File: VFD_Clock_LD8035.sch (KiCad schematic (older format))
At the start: 24 parts, among them J1 Conn_01x04, J2 Conn_01x04, J3 CONN_01X05, SW1 SW_Push, SW2 SW_Push, U1 74HC595_Misc, U2 TD62783, U3 TD62783

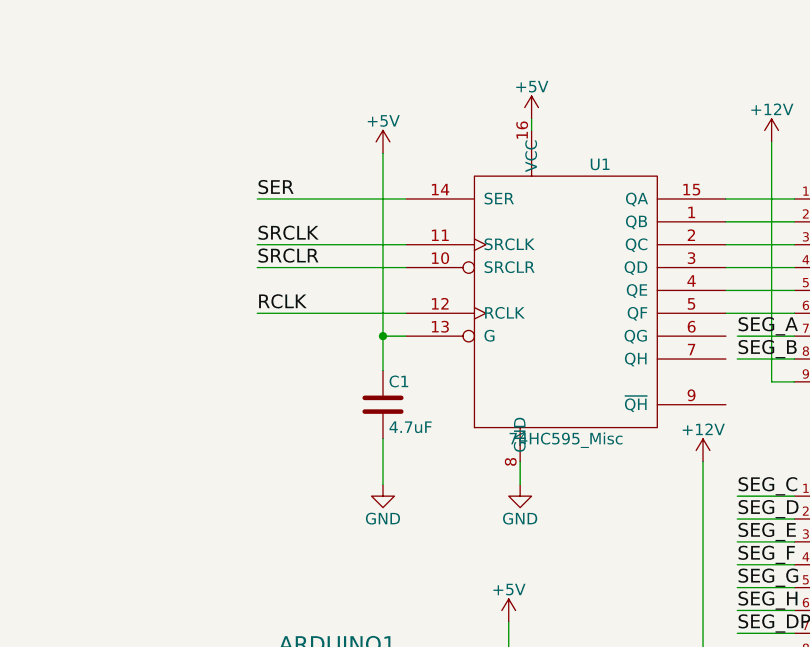
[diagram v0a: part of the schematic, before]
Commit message: Correct connection / Add dummy code
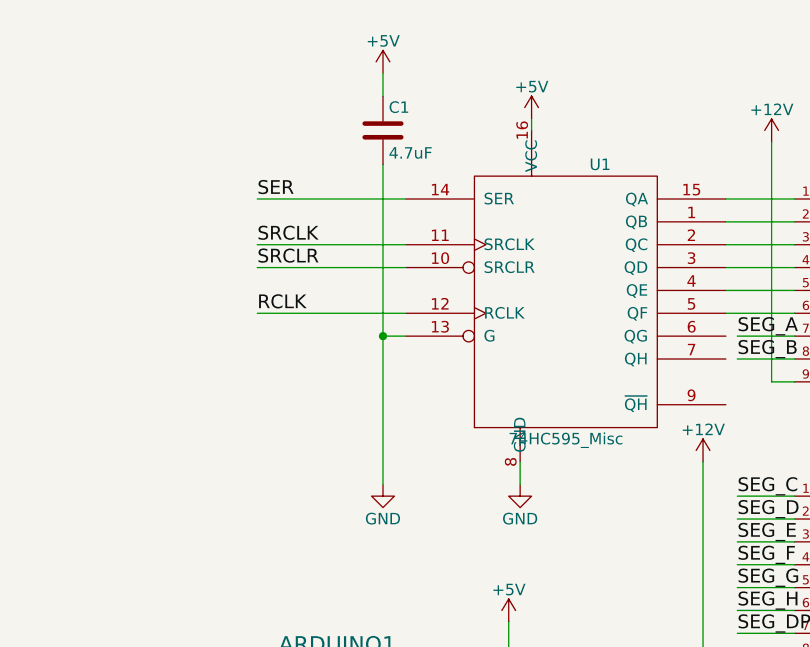
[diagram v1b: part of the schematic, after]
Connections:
- net +5V: no longer U1.13 (G)
- net GND: now also U1.13 (G)
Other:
- moved on the sheet: C1
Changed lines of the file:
@@
 L +5V #PWR019
 U 1 1 5AC41F8D
-P 3800 1050
-F 0 "#PWR019" H 3800 900 50  0001 C CNN
-F 1 "+5V" H 3800 1190 50  0000 C CNN
-F 2 "" H 3800 1050 50  0001 C CNN
-F 3 "" H 3800 1050 50  0001 C CNN
-	1    3800 1050
-	1    0    0    -1
-$EndComp
-Wire Wire Line
-	3800 1050 3800 2000
+P 3800 700
+F 0 "#PWR019" H 3800 550 50  0001 C CNN
+F 1 "+5V" H 3800 840 50  0000 C CNN
+F 2 "" H 3800 700 50  0001 C CNN
+F 3 "" H 3800 700 50  0001 C CNN
+	1    3800 700
+	1    0    0    -1
+$EndComp
 $Comp
 L +5V #PWR020
@@
 L C C1
 U 1 1 5AC4C0A0
-P 3800 2150
-F 0 "C1" H 3825 2250 50  0000 L CNN
-F 1 "4.7uF" H 3825 2050 50  0000 L CNN
-F 2 "Capacitors_THT:C_Disc_D7.5mm_W5.0mm_P5.00mm" H 3838 2000 50  0001 C CNN
-F 3 "" H 3800 2150 50  0001 C CNN
-	1    3800 2150
+P 3800 950
+F 0 "C1" H 3825 1050 50  0000 L CNN
+F 1 "4.7uF" H 3825 850 50  0000 L CNN
+F 2 "Capacitors_THT:C_Disc_D7.5mm_W5.0mm_P5.00mm" H 3838 800 50  0001 C CNN
+F 3 "" H 3800 950 50  0001 C CNN
+	1    3800 950
 	1    0    0    -1
 $EndComp
@@
 $EndComp
 Wire Wire Line
-	3800 2300 3800 2500
+	3800 1100 3800 2500
 $Comp
 L GND #PWR030
@@
 Text Notes 950  6400 0    60   ~ 0
 MT3608 Up Converter 5V to 12V
-Wire Wire Line
-	3900 1850 3800 1850
-Connection ~ 3800 1850
 $Comp
 L 74HC595_Misc U1
@@
 	1    0    0    -1
 $EndComp
+Wire Wire Line
+	3800 800  3800 700
+Wire Wire Line
+	3900 1850 3800 1850
+Connection ~ 3800 1850
 $EndSCHEMATC

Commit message: Changed Resistor to 1/2W
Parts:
- R1, R2, R3, R4, R5, R6: footprint Resistors_THT:R_Axial_DIN0207_L6.3mm_D2.5mm_P2.54mm_Vertical -> Resistors_THT:R_Axial_DIN0309_L9.0mm_D3.2mm_P5.08mm_Vertical
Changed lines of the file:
@@
 F 0 "R1" V 8930 800 50  0000 C CNN
 F 1 "R" V 8850 800 50  0000 C CNN
-F 2 "Resistors_THT:R_Axial_DIN0207_L6.3mm_D2.5mm_P2.54mm_Vertical" V 8780 800 50  0001 C CNN
+F 2 "Resistors_THT:R_Axial_DIN0309_L9.0mm_D3.2mm_P5.08mm_Vertical" V 8780 800 50  0001 C CNN
 F 3 "" H 8850 800 50  0001 C CNN
 	1    8850 800
@@
 F 0 "R2" V 8930 2000 50  0000 C CNN
 F 1 "R" V 8850 2000 50  0000 C CNN
-F 2 "Resistors_THT:R_Axial_DIN0207_L6.3mm_D2.5mm_P2.54mm_Vertical" V 8780 2000 50  0001 C CNN
+F 2 "Resistors_THT:R_Axial_DIN0309_L9.0mm_D3.2mm_P5.08mm_Vertical" V 8780 2000 50  0001 C CNN
 F 3 "" H 8850 2000 50  0001 C CNN
 	1    8850 2000
@@
 F 0 "R3" V 8930 3200 50  0000 C CNN
 F 1 "R" V 8850 3200 50  0000 C CNN
-F 2 "Resistors_THT:R_Axial_DIN0207_L6.3mm_D2.5mm_P2.54mm_Vertical" V 8780 3200 50  0001 C CNN
+F 2 "Resistors_THT:R_Axial_DIN0309_L9.0mm_D3.2mm_P5.08mm_Vertical" V 8780 3200 50  0001 C CNN
 F 3 "" H 8850 3200 50  0001 C CNN
 	1    8850 3200
@@
 F 0 "R4" V 8930 4450 50  0000 C CNN
 F 1 "R" V 8850 4450 50  0000 C CNN
-F 2 "Resistors_THT:R_Axial_DIN0207_L6.3mm_D2.5mm_P2.54mm_Vertical" V 8780 4450 50  0001 C CNN
+F 2 "Resistors_THT:R_Axial_DIN0309_L9.0mm_D3.2mm_P5.08mm_Vertical" V 8780 4450 50  0001 C CNN
 F 3 "" H 8850 4450 50  0001 C CNN
 	1    8850 4450
@@
 F 0 "R5" V 10780 800 50  0000 C CNN
 F 1 "R" V 10700 800 50  0000 C CNN
-F 2 "Resistors_THT:R_Axial_DIN0207_L6.3mm_D2.5mm_P2.54mm_Vertical" V 10630 800 50  0001 C CNN
+F 2 "Resistors_THT:R_Axial_DIN0309_L9.0mm_D3.2mm_P5.08mm_Vertical" V 10630 800 50  0001 C CNN
 F 3 "" H 10700 800 50  0001 C CNN
 	1    10700 800
@@
 F 0 "R6" V 10780 2000 50  0000 C CNN
 F 1 "R" V 10700 2000 50  0000 C CNN
-F 2 "Resistors_THT:R_Axial_DIN0207_L6.3mm_D2.5mm_P2.54mm_Vertical" V 10630 2000 50  0001 C CNN
+F 2 "Resistors_THT:R_Axial_DIN0309_L9.0mm_D3.2mm_P5.08mm_Vertical" V 10630 2000 50  0001 C CNN
 F 3 "" H 10700 2000 50  0001 C CNN
 	1    10700 2000

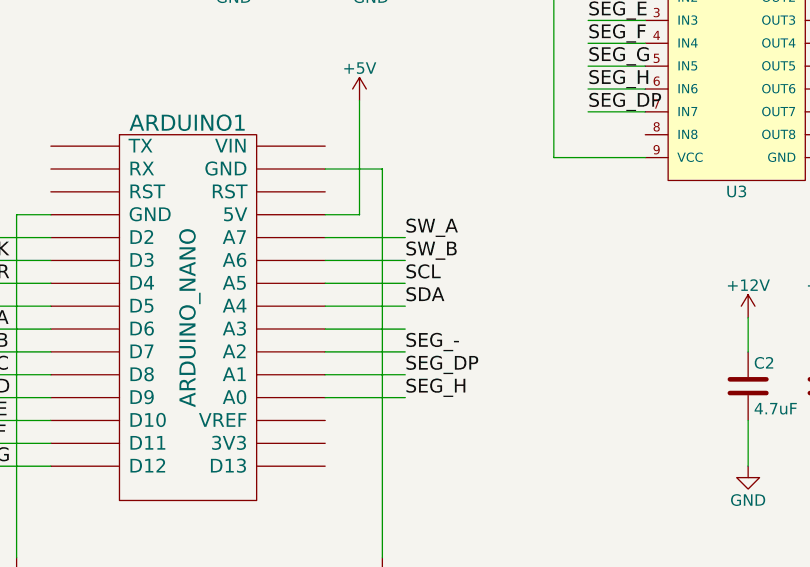
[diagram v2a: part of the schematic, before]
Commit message: Changed button connection RTC implement
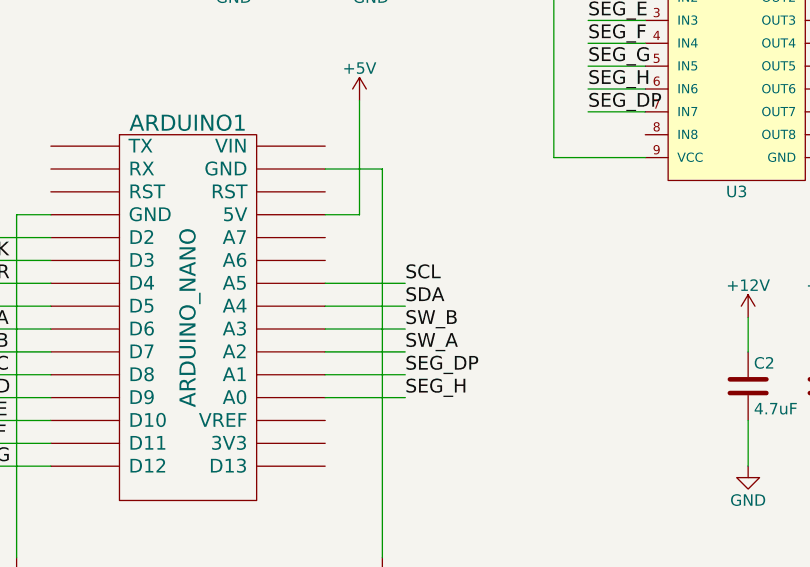
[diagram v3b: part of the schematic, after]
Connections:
- net SEG_- is gone; now on net SW_A: ARDUINO1.21 (A2)
- net SW_A: no longer ARDUINO1.26 (A7)
- net SW_B: now also ARDUINO1.22 (A3); no longer ARDUINO1.25 (A6)
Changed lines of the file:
@@
 Wire Wire Line
 	4200 4300 4550 4300
-Text Label 4550 4200 0    60   ~ 0
-SEG_-
-Wire Wire Line
-	4200 4200 4550 4200
 Text Label 4550 4000 0    60   ~ 0
 SDA
@@
 Wire Wire Line
 	4200 3900 4550 3900
-Wire Wire Line
-	4200 4100 4550 4100
-Wire Wire Line
-	4200 3700 4550 3700
-Wire Wire Line
-	4200 3800 4550 3800
-Text Label 4550 3700 0    60   ~ 0
+Text Label 4550 4200 0    60   ~ 0
 SW_A
-Text Label 4550 3800 0    60   ~ 0
+Text Label 4550 4100 0    60   ~ 0
 SW_B
 $Comp
@@
 	3900 1850 3800 1850
 Connection ~ 3800 1850
+Wire Wire Line
+	4200 4100 4550 4100
+Wire Wire Line
+	4200 4200 4550 4200
 $EndSCHEMATC

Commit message: Updated schematics / board
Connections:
- net +12V: no longer R1.2, R2.2, R3.2, R4.2, R5.2, R6.2
- net +5V: now also R1.2, R2.2, R3.2, R4.2, R5.2, R6.2
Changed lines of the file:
@@
 Wire Wire Line
 	9050 4800 9050 5400
-$Comp
-L +12V #PWR07
-U 1 1 5AC3BF1A
-P 9300 650
-F 0 "#PWR07" H 9300 500 50  0001 C CNN
-F 1 "+12V" H 9300 790 50  0000 C CNN
-F 2 "" H 9300 650 50  0001 C CNN
-F 3 "" H 9300 650 50  0001 C CNN
-	1    9300 650
-	1    0    0    -1
-$EndComp
-$Comp
-L +12V #PWR08
-U 1 1 5AC3C0DD
-P 9300 1950
-F 0 "#PWR08" H 9300 1800 50  0001 C CNN
-F 1 "+12V" H 9300 2090 50  0000 C CNN
-F 2 "" H 9300 1950 50  0001 C CNN
-F 3 "" H 9300 1950 50  0001 C CNN
-	1    9300 1950
-	1    0    0    -1
-$EndComp
-$Comp
-L +12V #PWR09
-U 1 1 5AC3C17B
-P 9300 3150
-F 0 "#PWR09" H 9300 3000 50  0001 C CNN
-F 1 "+12V" H 9300 3290 50  0000 C CNN
-F 2 "" H 9300 3150 50  0001 C CNN
-F 3 "" H 9300 3150 50  0001 C CNN
-	1    9300 3150
-	1    0    0    -1
-$EndComp
-$Comp
-L +12V #PWR010
-U 1 1 5AC3C28C
-P 9300 4400
-F 0 "#PWR010" H 9300 4250 50  0001 C CNN
-F 1 "+12V" H 9300 4540 50  0000 C CNN
-F 2 "" H 9300 4400 50  0001 C CNN
-F 3 "" H 9300 4400 50  0001 C CNN
-	1    9300 4400
-	1    0    0    -1
-$EndComp
 Wire Wire Line
 	9000 2350 9050 2350
@@
 Wire Wire Line
 	10350 800  10550 800
-$Comp
-L +12V #PWR011
-U 1 1 5AC3C7CB
-P 11050 650
-F 0 "#PWR011" H 11050 500 50  0001 C CNN
-F 1 "+12V" H 11050 790 50  0000 C CNN
-F 2 "" H 11050 650 50  0001 C CNN
-F 3 "" H 11050 650 50  0001 C CNN
-	1    11050 650
-	1    0    0    -1
-$EndComp
-$Comp
-L +12V #PWR012
-U 1 1 5AC3C815
-P 11100 1950
-F 0 "#PWR012" H 11100 1800 50  0001 C CNN
-F 1 "+12V" H 11100 2090 50  0000 C CNN
-F 2 "" H 11100 1950 50  0001 C CNN
-F 3 "" H 11100 1950 50  0001 C CNN
-	1    11100 1950
-	1    0    0    -1
-$EndComp
 Wire Wire Line
 	9000 800  9300 800
@@
 Wire Wire Line
 	4200 4200 4550 4200
+$Comp
+L +5V #PWR?
+U 1 1 5B0E28B7
+P 9300 650
+F 0 "#PWR?" H 9300 500 50  0001 C CNN
+F 1 "+5V" H 9300 790 50  0000 C CNN
+F 2 "" H 9300 650 50  0001 C CNN
+F 3 "" H 9300 650 50  0001 C CNN
+	1    9300 650
+	1    0    0    -1
+$EndComp
+$Comp
+L +5V #PWR?
+U 1 1 5B0E2A72
+P 9300 1950
+F 0 "#PWR?" H 9300 1800 50  0001 C CNN
+F 1 "+5V" H 9300 2090 50  0000 C CNN
+F 2 "" H 9300 1950 50  0001 C CNN
+F 3 "" H 9300 1950 50  0001 C CNN
+	1    9300 1950
+	1    0    0    -1
+$EndComp
+$Comp
+L +5V #PWR?
+U 1 1 5B0E2E85
+P 9300 3150
+F 0 "#PWR?" H 9300 3000 50  0001 C CNN
+F 1 "+5V" H 9300 3290 50  0000 C CNN
+F 2 "" H 9300 3150 50  0001 C CNN
+F 3 "" H 9300 3150 50  0001 C CNN
+	1    9300 3150
+	1    0    0    -1
+$EndComp
+$Comp
+L +5V #PWR?
+U 1 1 5B0E2ED8
+P 9300 4400
+F 0 "#PWR?" H 9300 4250 50  0001 C CNN
+F 1 "+5V" H 9300 4540 50  0000 C CNN
+F 2 "" H 9300 4400 50  0001 C CNN
+F 3 "" H 9300 4400 50  0001 C CNN
+	1    9300 4400
+	1    0    0    -1
+$EndComp
+$Comp
+L +5V #PWR?
+U 1 1 5B0E2F2B
+P 11050 650
+F 0 "#PWR?" H 11050 500 50  0001 C CNN
+F 1 "+5V" H 11050 790 50  0000 C CNN
+F 2 "" H 11050 650 50  0001 C CNN
+F 3 "" H 11050 650 50  0001 C CNN
+	1    11050 650
+	1    0    0    -1
+$EndComp
+$Comp
+L +5V #PWR?
+U 1 1 5B0E324E
+P 11100 1950
+F 0 "#PWR?" H 11100 1800 50  0001 C CNN
+F 1 "+5V" H 11100 2090 50  0000 C CNN
+F 2 "" H 11100 1950 50  0001 C CNN
+F 3 "" H 11100 1950 50  0001 C CNN
+	1    11100 1950
+	1    0    0    -1
+$EndComp
 $EndSCHEMATC

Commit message: Some fixes for Code
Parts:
- removed C1: 4.7uF, Capacitors_THT:C_Disc_D7.5mm_W5.0mm_P5.00mm, symbol C
- removed U1: 74HC595_Misc, Housings_DIP:DIP-16_W7.62mm_LongPads, symbol 74HC595_Misc
- R1, R2, R3, R4, R5, R6: value R -> 200
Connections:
- net RCLK is gone; now on net DIGIT_2_AR: ARDUINO1.8 (D5)
- net SER is gone; now on net DIGIT_5_AR: ARDUINO1.5 (D2)
- net SRCLK is gone; now on net SW_A: ARDUINO1.6 (D3)
- net SRCLR is gone; now on net SW_B: ARDUINO1.7 (D4)
- net SEG_H: no longer ARDUINO1.19 (A0)
- net SW_A: no longer ARDUINO1.21 (A2)
- net SW_B: no longer ARDUINO1.22 (A3)
- net DIGIT_3_AR: now reaches ARDUINO1.16 (D13)
- net DIGIT_3_AR: now also U2.4 (IN4)
- net DIGIT_0_AR: now reaches U2.1 (IN1)
- net DIGIT_0_AR: now also ARDUINO1.21 (A2)
- net DIGIT_1_AR: now reaches U2.2 (IN2)
- net DIGIT_1_AR: now also ARDUINO1.22 (A3)
- net DIGIT_2_AR: now reaches U2.3 (IN3)
- net DIGIT_4_AR: now reaches U2.5 (IN5)
- net DIGIT_4_AR: now also ARDUINO1.19 (A0)
- net DIGIT_5_AR: now reaches U2.6 (IN6)
- no-connect marks 0 -> 15
